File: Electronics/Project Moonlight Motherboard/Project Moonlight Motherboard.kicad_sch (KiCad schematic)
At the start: 31 parts, among them CN10 B2B-XH-A, CN11 B2B-XH-A, CN12 B2B-XH-A, CN5 1751248, CN6 1751248, CN7 B2B-XH-A, CN8 B2B-XH-A, CN9 B2B-XH-A, Q1 AO3400A, Q2 AO3400A, Q3 AO3400A, U1 Pico, U2 TMC2209_SILENTSTEPSTICK, U3 TMC2209_SILENTSTEPSTICK, U4 TMC2209_SILENTSTEPSTICK, U5 TMC2209_SILENTSTEPSTICK

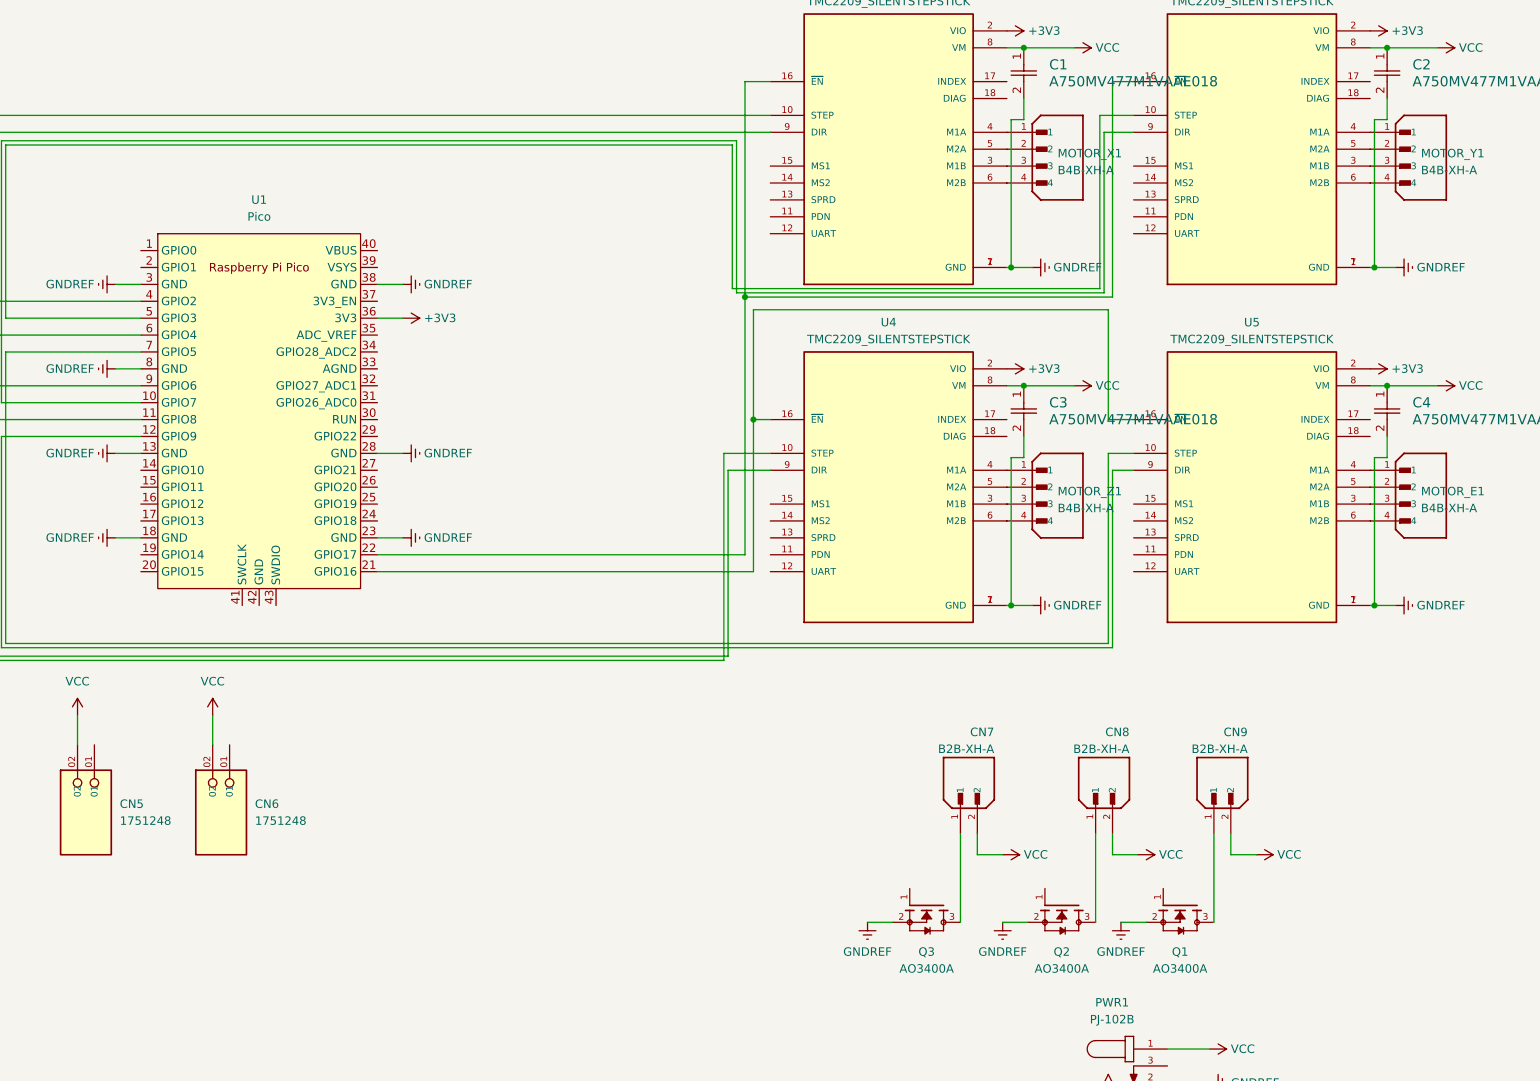
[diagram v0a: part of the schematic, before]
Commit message: reorganized schematic and updated refs + routing
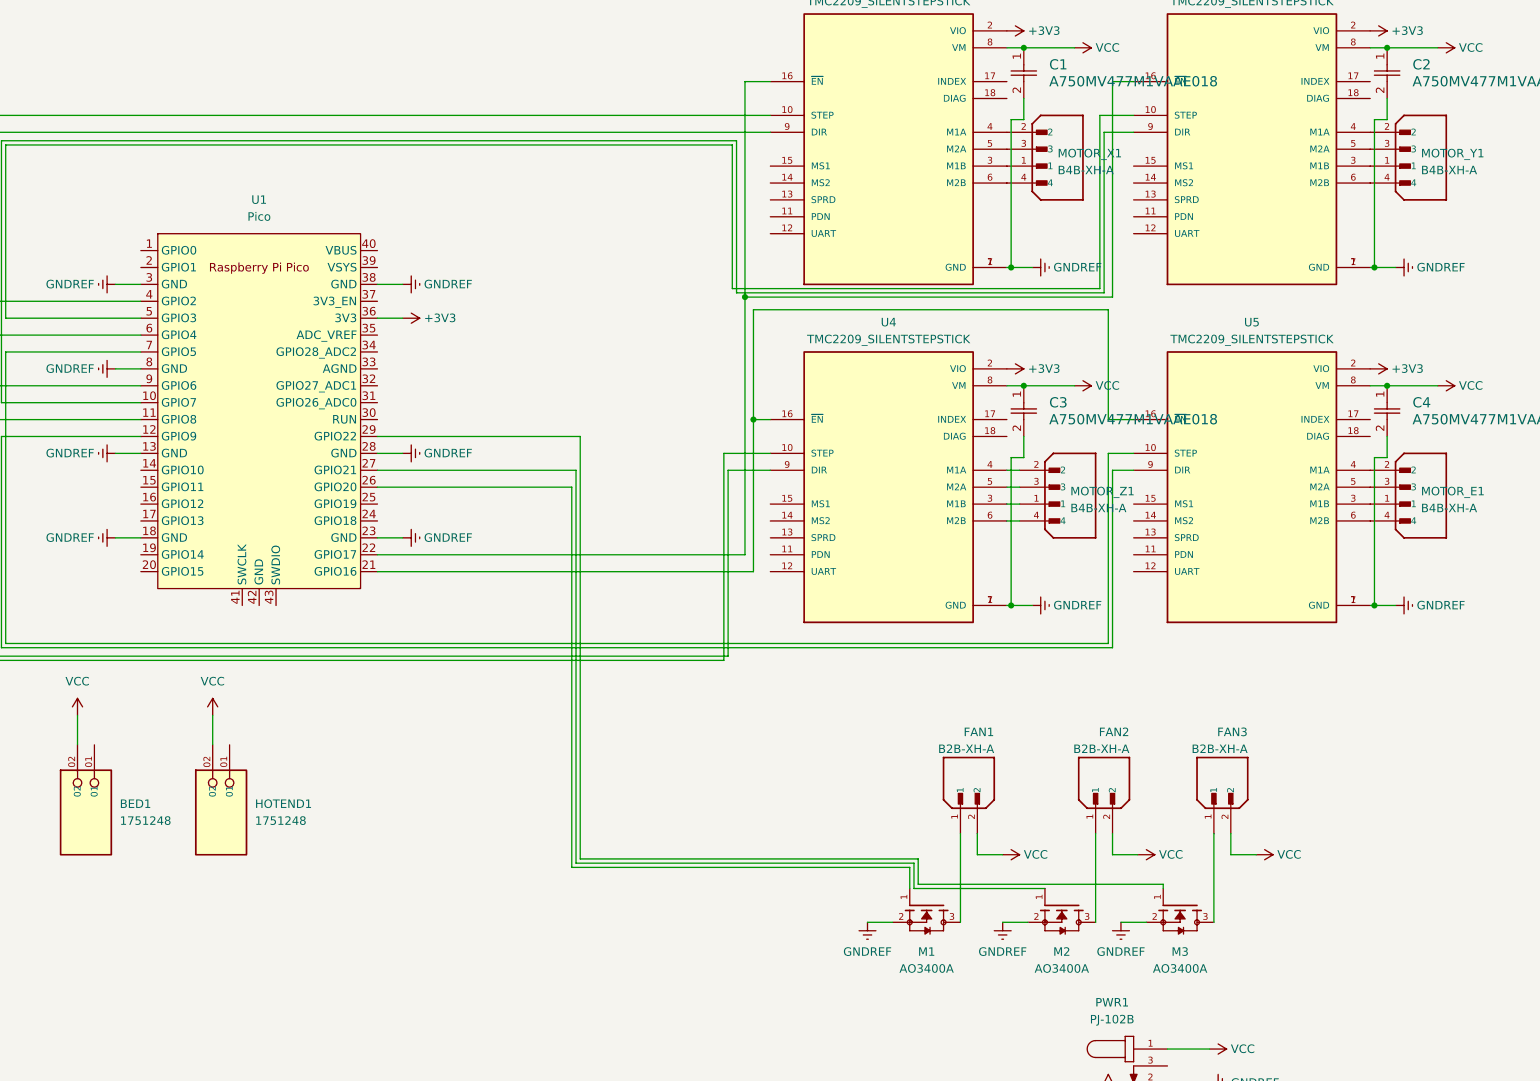
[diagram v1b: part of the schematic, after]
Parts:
- renumbered CN5 to BED1, CN7 to FAN1, CN8 to FAN2, CN9 to FAN3, CN6 to HOTEND1, Q3 to M1, Q2 to M2, Q1 to M3
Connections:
- net at U2.3 (M1B): now also MOTOR_X1.1; no longer MOTOR_X1.3
- net at U2.4 (M1A): now also MOTOR_X1.2; no longer MOTOR_X1.1
- net at U2.5 (M2A): now also MOTOR_X1.3; no longer MOTOR_X1.2
- net at U4.3 (M1B): now also MOTOR_Z1.1; no longer MOTOR_Z1.3
- net at U4.4 (M1A): now also MOTOR_Z1.2; no longer MOTOR_Z1.1
- net at U4.5 (M2A): now also MOTOR_Z1.3; no longer MOTOR_Z1.2
- net at M1.1: now also U1.26 (GPIO20)
- net at U5.3 (M1B): now also MOTOR_E1.1; no longer MOTOR_E1.3
- net at U5.4 (M1A): now also MOTOR_E1.2; no longer MOTOR_E1.1
- net at U5.5 (M2A): now also MOTOR_E1.3; no longer MOTOR_E1.2
- net at M2.1: now also U1.27 (GPIO21)
- net at U3.3 (M1B): now also MOTOR_Y1.1; no longer MOTOR_Y1.3
- net at U3.4 (M1A): now also MOTOR_Y1.2; no longer MOTOR_Y1.1
- net at U3.5 (M2A): now also MOTOR_Y1.3; no longer MOTOR_Y1.2
- net at M3.1: now also U1.29 (GPIO22)
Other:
- moved on the sheet: MOTOR_Z1

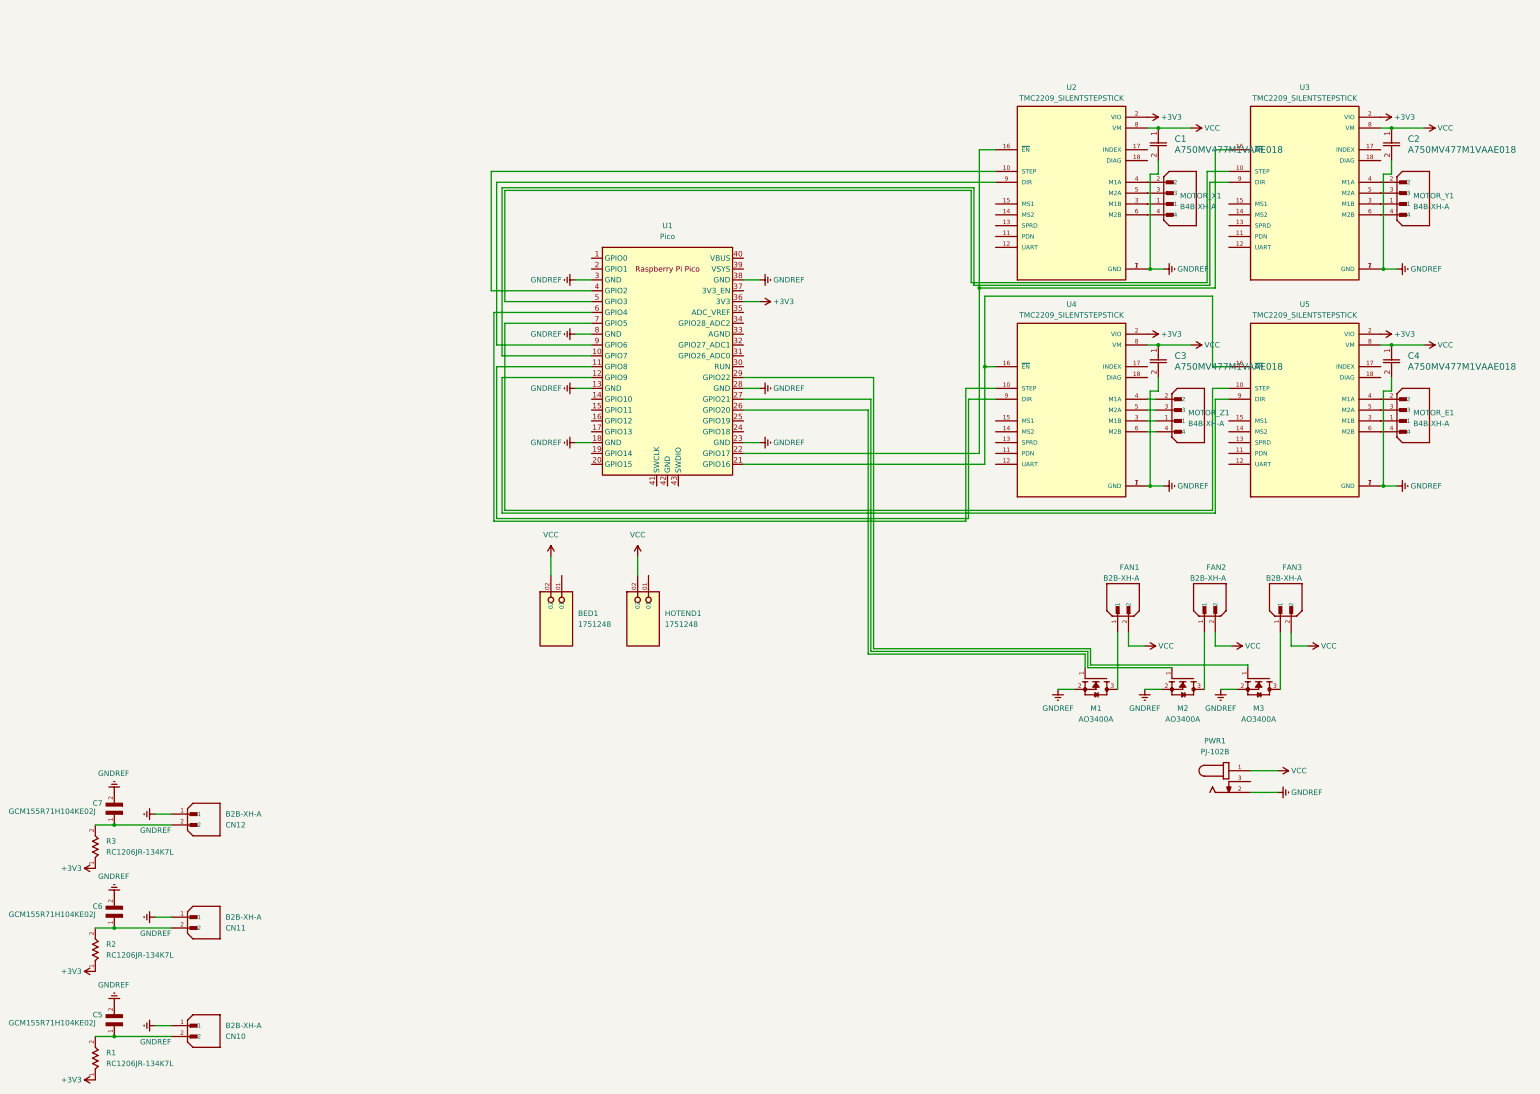
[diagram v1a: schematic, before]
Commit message: added power MOSFETs for hotend and bed
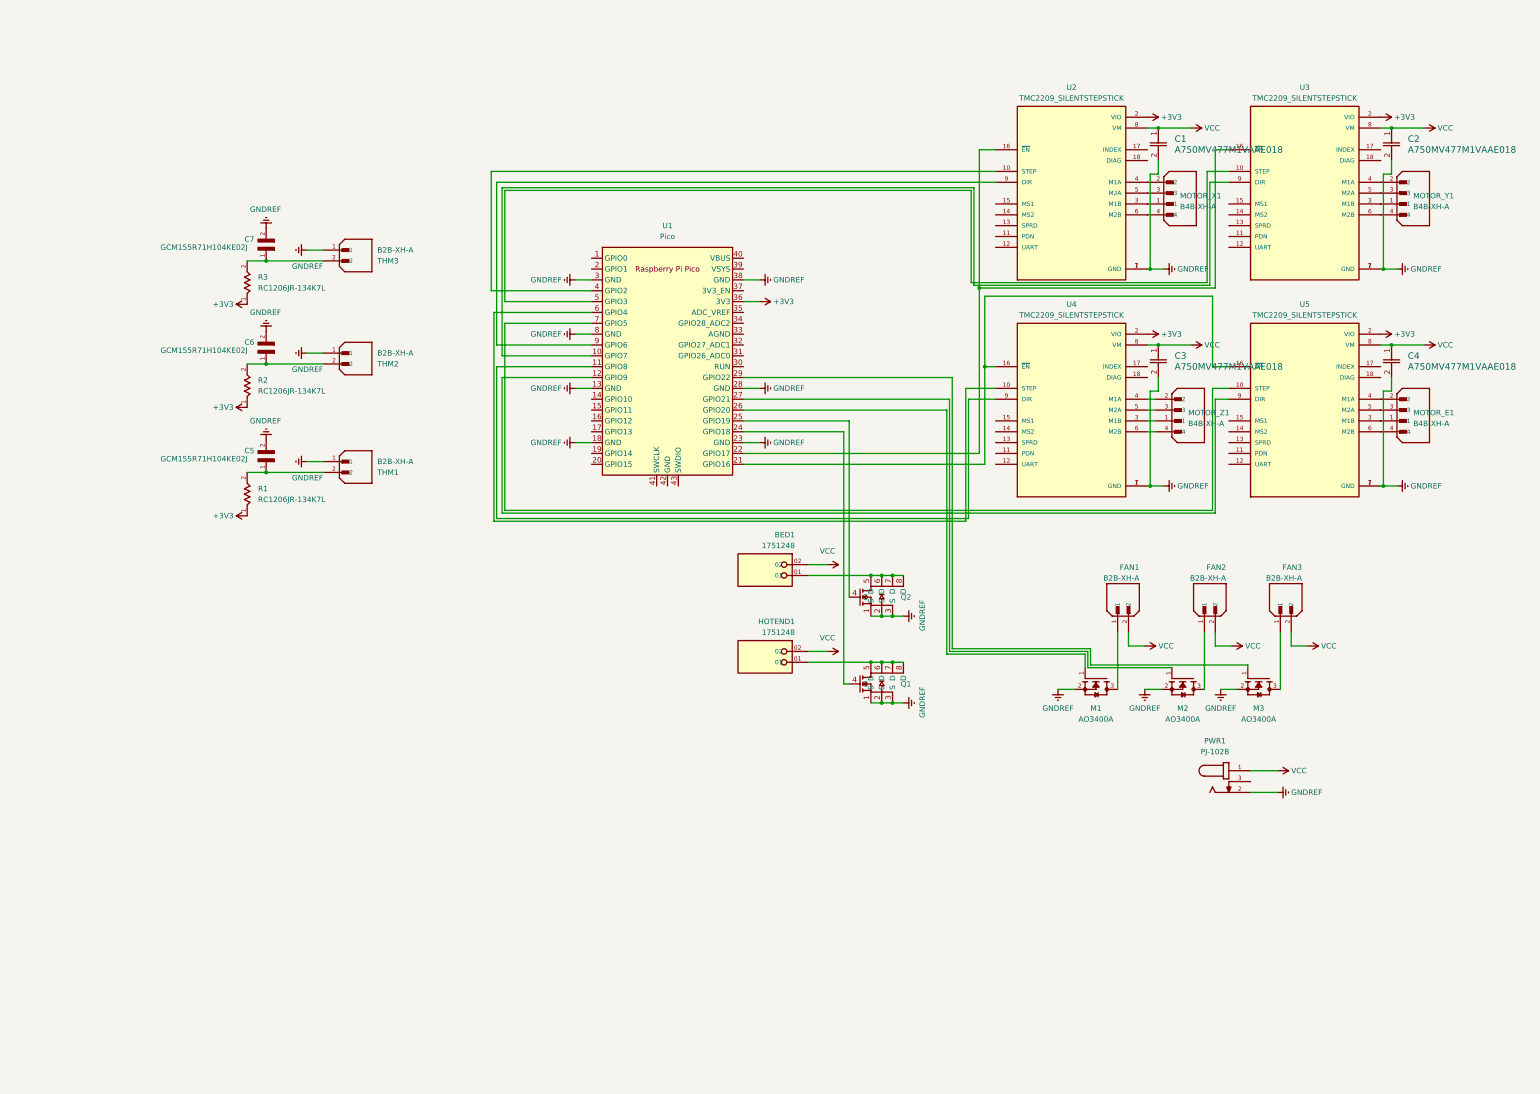
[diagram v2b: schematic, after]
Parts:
- added Q1, Q2: ~, IRFH7440TRPBF:TRANS_FDMS86202, symbol IRFH7440TRPBF:IRFH7440TRPBF
- renumbered CN10 to THM1, CN11 to THM2, CN12 to THM3
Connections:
- net GNDREF: now also Q1.1 (S), Q1.2 (S), Q1.3 (S), Q2.1 (S), Q2.2 (S), Q2.3 (S)
- net at BED1.01: now also Q2.5 (D), Q2.6 (D), Q2.7 (D), Q2.8 (D)
- net at HOTEND1.01: now also Q1.5 (D), Q1.6 (D), Q1.7 (D), Q1.8 (D)
- net at U1.24 (GPIO18): now also Q1.4 (G)
- net at U1.25 (GPIO19): now also Q2.4 (G)
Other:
- moved on the sheet: BED1, C5, C6, C7, HOTEND1, R1, R2, R3, THM1, THM2, THM3

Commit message: added headers for screen and rotary encoder, more tweaks
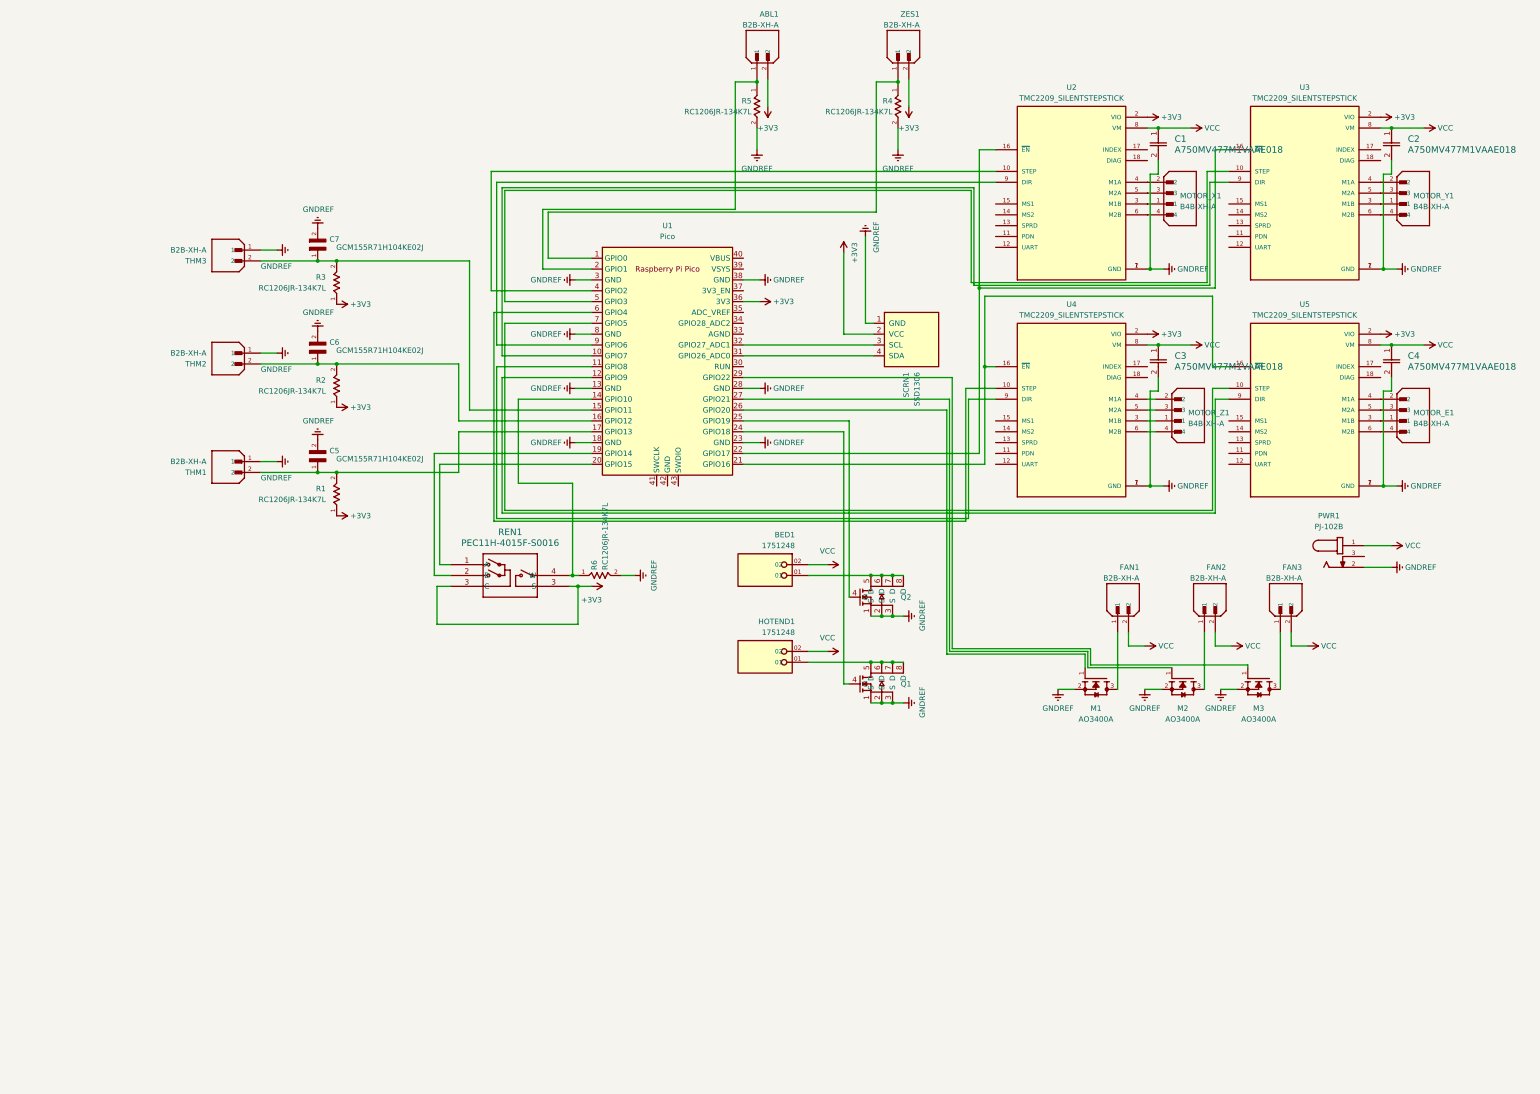
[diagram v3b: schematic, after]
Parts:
- added ABL1, ZES1: B2B-XH-A, B2B-XH-A:JST_B2B-XH-A, symbol B2B-XH-A:B2B-XH-A
- added R4, R5, R6: RC1206JR-134K7L, RC1206JR-134K7L:RESC3216X65, symbol RC1206JR-134K7L:RC1206JR-134K7L
- added REN1: PEC11H-4015F-S0016, Connector_PinHeader_2.54mm:PinHeader_1x04_P2.54mm_Vertical, symbol PEC11H-4015F-S0016:PEC11H-4015F-S0016
- added SCRN1: SSD1306, Connector_PinHeader_2.54mm:PinHeader_1x04_P2.54mm_Vertical, symbol SSD1306-128x64_OLED:SSD1306
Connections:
- net +3V3: now also ABL1.2, REN1.3 (S), SCRN1.2 (VCC), ZES1.2
- net GNDREF: now also R4.2, R5.2, R6.2, SCRN1.1 (GND)
- net at C6.1, R2.2, THM2.2: now also U1.16 (GPIO12)
- net at C5.1, R1.2, THM1.2: now also U1.17 (GPIO13)
- net at C7.1, R3.2, THM3.2: now also U1.15 (GPIO11)
- net at U1.1 (GPIO0): now also R4.1, ZES1.1
- net at U1.14 (GPIO10): now also R6.1, REN1.4 (W)
- net at U1.19 (GPIO14): now also REN1.2 (B)
- net at U1.2 (GPIO1): now also ABL1.1, R5.1
- net at U1.20 (GPIO15): now also REN1.1 (A)
- net at U1.31 (GPIO26_ADC0): now also SCRN1.4 (SDA)
- net at U1.32 (GPIO27_ADC1): now also SCRN1.3 (SCL)
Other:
- moved on the sheet: C5, C6, C7, PWR1, R1, R2, R3, THM1, THM2, THM3
